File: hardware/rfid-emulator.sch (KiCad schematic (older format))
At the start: 95 parts, among them J1 AVR-JTAG-10, J2 Micro_USB, J3 OSTTC020162, Q1 2N3904, Q2 2N3906, Q3 2N3906, Q4 IRLML6344TRPBF, Q5 IRLML6344TRPBF, SW1 EN11-HSM1BF20, U1 NHD-C0216CiZ-FSW-FBW-3V3, U2 LT8613, U3 ATmega64A-AU, U4 MCP73832-2-OT, U5 LF33_TO252, U6 FT230XS, U7 LM324DT, Y1 ECS-160-20-5PX-TR

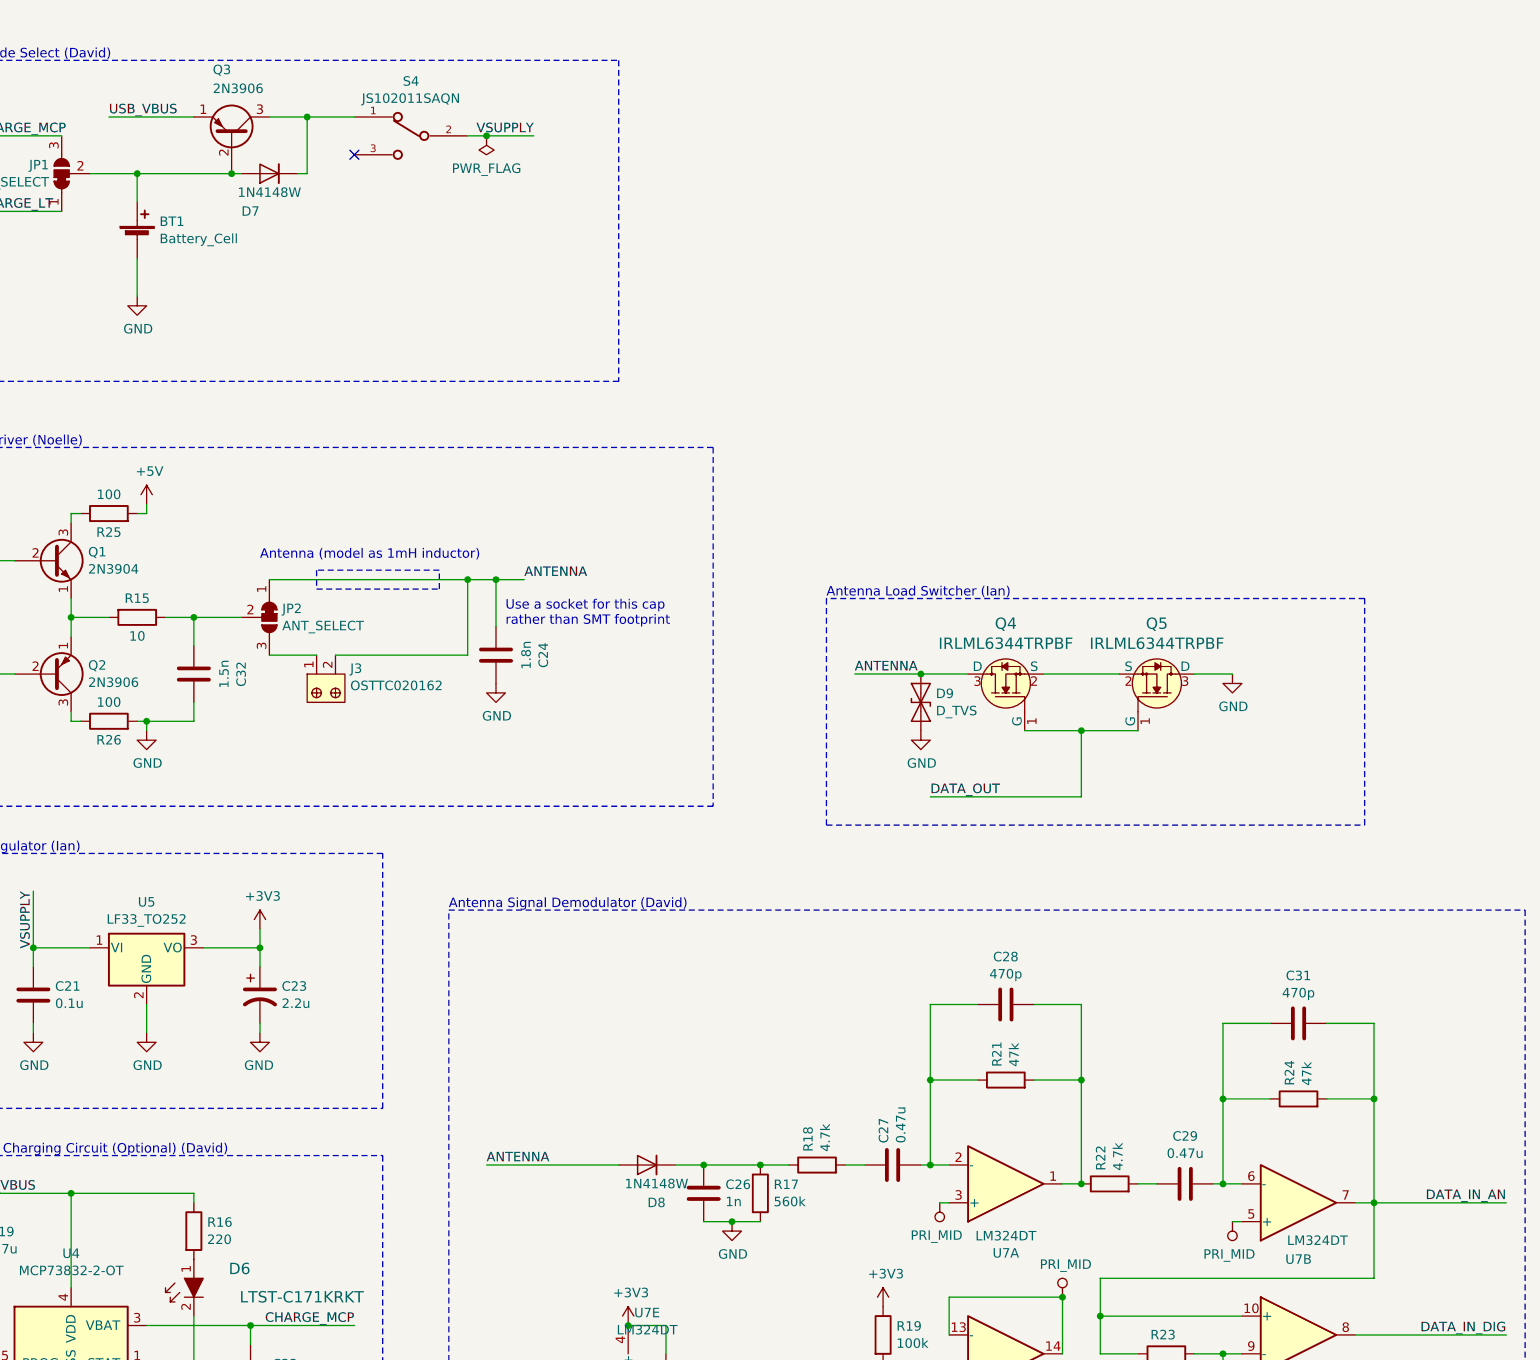
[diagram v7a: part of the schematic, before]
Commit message: Add test points and extra capacitor socket
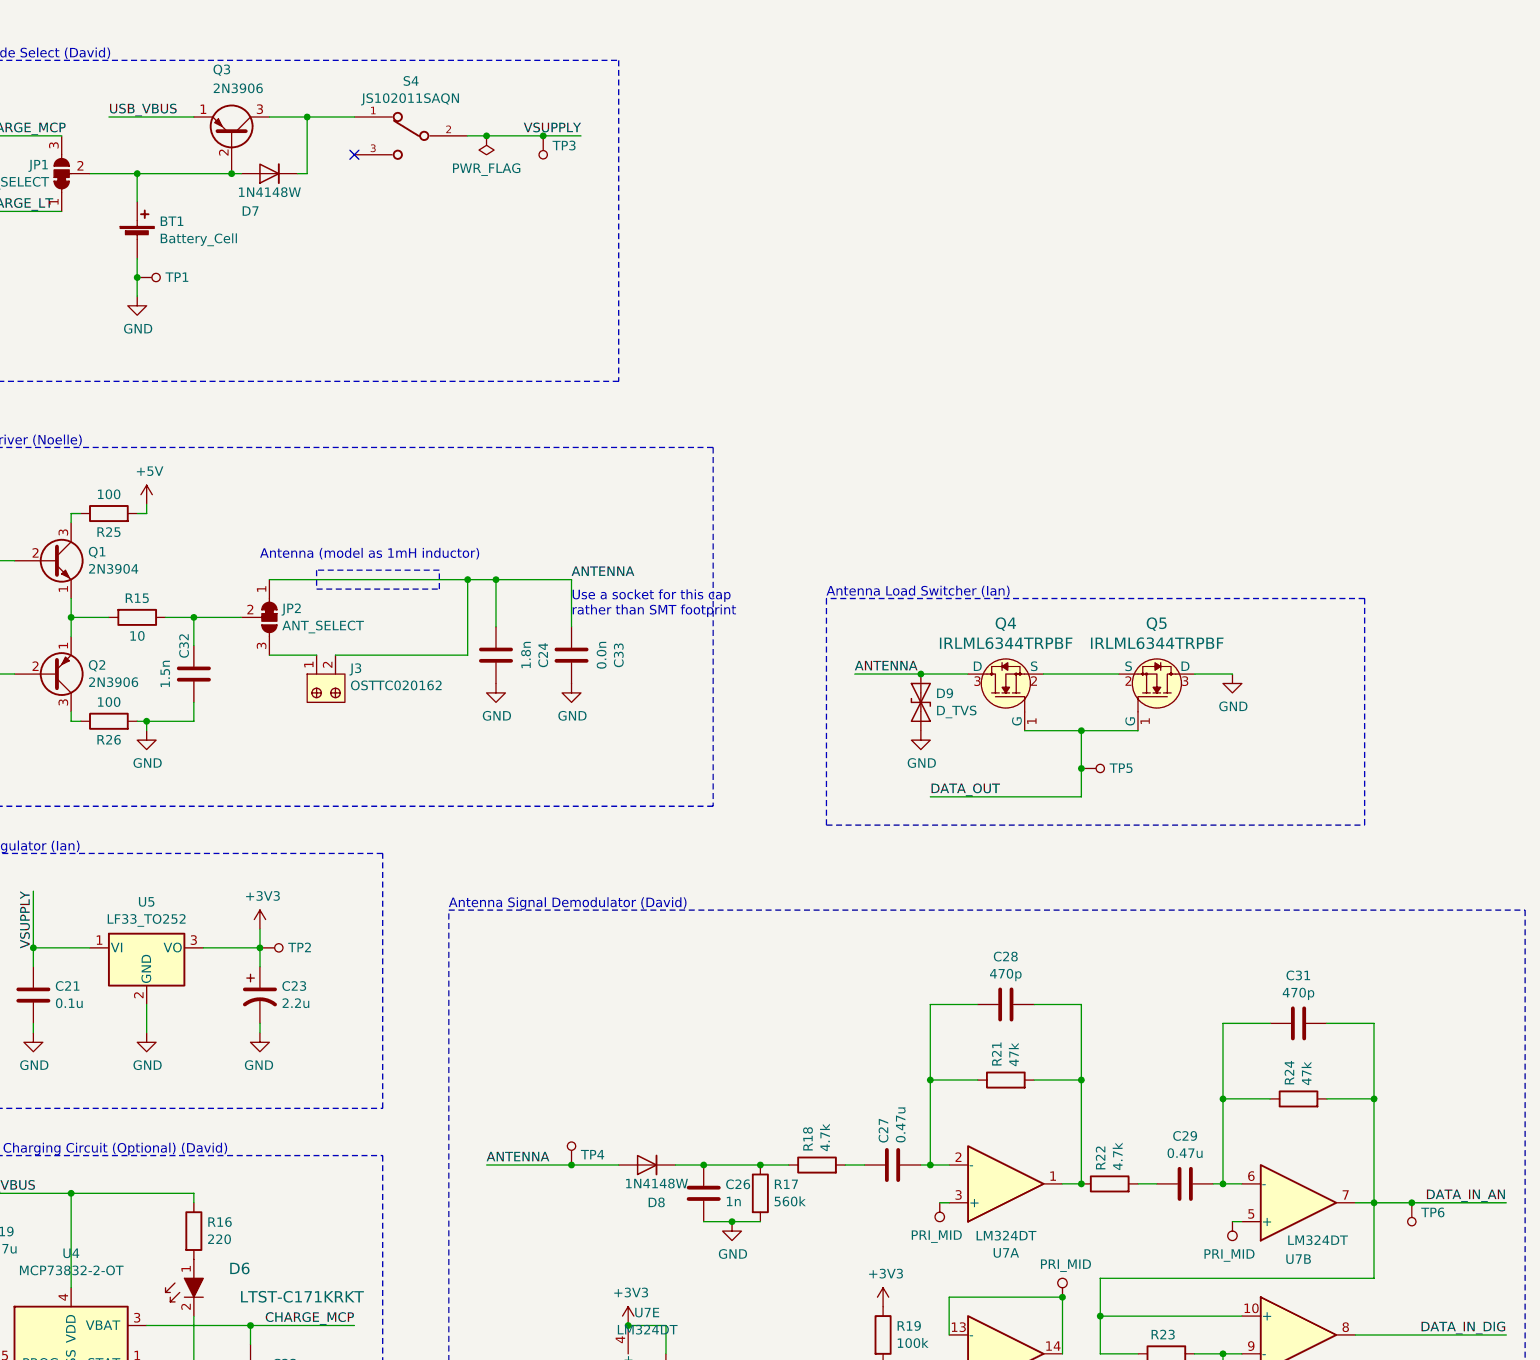
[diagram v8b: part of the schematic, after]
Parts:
- added C33: 0.0n, Socket_Strips:Socket_Strip_Straight_1x02_Pitch2.54mm, symbol Device:C
- added TP1: 5001, digikey-footprints:Test_Point_D1.02mm, symbol dk_Test-Points:5001
- added TP2, TP3: 5000, digikey-footprints:Test_Point_D1.02mm, symbol dk_Test-Points:5000
- added TP4, TP5, TP6: 5002, digikey-footprints:Test_Point_D1.02mm, symbol dk_Test-Points:5002
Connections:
- net +3V3: now also TP2.1
- net ANTENNA: now also C33.2, TP4.1
- net DATA_IN_AN: now also TP6.1
- net DATA_OUT: now also TP5.1
- net GND: now also C33.1, TP1.1
- net VSUPPLY: now also TP3.1
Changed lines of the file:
@@
 	-1   0    0    1
 $EndComp
-Text Label 10200 3650 0    50   ~ 0
+Text Label 10450 3650 0    50   ~ 0
 ANTENNA
 Wire Wire Line
-	10200 3650 10050 3650
+	10450 3650 10050 3650
 Text Label 7150 3850 0    50   ~ 0
 OC0
@@
 Wire Wire Line
 	13750 4150 13950 4150
-Wire Wire Line
-	13150 4800 13150 4450
 Wire Wire Line
 	12350 4800 13150 4800
@@
 	0    -1   -1   0
 $EndComp
-Text Notes 10100 3900 0    50   ~ 0
+Text Notes 10450 3850 0    50   ~ 0
 Use a socket for this cap\nrather than SMT footprint
 $Comp
@@
 Text Label 7250 6900 0    50   ~ 0
 USB_VBUS
-Text Label 10250 1300 2    50   ~ 0
+Text Label 10500 1300 2    50   ~ 0
 VSUPPLY
 Wire Wire Line
@@
 $EndComp
 Wire Wire Line
-	10000 6750 10700 6750
-Wire Wire Line
 	12450 7450 13050 7450
 Wire Wire Line
 	14600 7650 15400 7650
 Wire Wire Line
-	14700 6950 15400 6950
-Wire Wire Line
 	8500 5600 8800 5600
 Wire Wire Line
 	9050 1200 9300 1200
 Wire Wire Line
-	10250 1300 10000 1300
+	10500 1300 10300 1300
 Connection ~ 10000 1300
 Wire Wire Line
@@
 $EndComp
 Wire Wire Line
-	8150 1950 8150 2150
+	8150 1950 8150 2050
 Wire Wire Line
 	12300 6750 12350 6750
@@
 U 1 1 5DD510A8
 P 8450 4150
-F 0 "C32" V 8198 4150 50  0000 C CNN
-F 1 "1.5n" V 8289 4150 50  0000 C CNN
+F 0 "C32" V 8500 4000 50  0000 C CNN
+F 1 "1.5n" V 8600 4150 50  0000 C CNN
 F 2 "Capacitors_SMD:C_0805_HandSoldering" H 8488 4000 50  0001 C CNN
 F 3 "~" H 8450 4150 50  0001 C CNN
@@
 Text Notes 8800 3550 0    50   ~ 0
 Antenna (model as 1mH inductor)
+Connection ~ 8150 2050
+Wire Wire Line
+	8150 2050 8150 2150
+$Comp
+L dk_Test-Points:5001 TP1
+U 1 1 5DEB6467
+P 8250 2050
+F 0 "TP1" V 8250 2000 50  0000 R CNN
+F 1 "5001" H 8250 1950 50  0001 C CNN
+F 2 "digikey-footprints:Test_Point_D1.02mm" H 8450 2250 60  0001 L CNN
+F 3 "http://www.keyelco.com/product-pdf.cfm?p=1310" H 8450 2350 60  0001 L CNN
+F 4 "36-5001-ND" H 8450 2450 60  0001 L CNN "Digi-Key_PN"
+F 5 "5001" H 8450 2550 60  0001 L CNN "MPN"
+F 6 "Test and Measurement" H 8450 2650 60  0001 L CNN "Category"
+F 7 "Test Points" H 8450 2750 60  0001 L CNN "Family"
+F 8 "http://www.keyelco.com/product-pdf.cfm?p=1310" H 8450 2850 60  0001 L CNN "DK_Datasheet_Link"
+F 9 "/product-detail/en/keystone-electronics/5001/36-5001-ND/255327" H 8450 2950 60  0001 L CNN "DK_Detail_Page"
+F 10 "PC TEST POINT MINIATURE BLACK" H 8450 3050 60  0001 L CNN "Description"
+F 11 "Keystone Electronics" H 8450 3150 60  0001 L CNN "Manufacturer"
+F 12 "Active" H 8450 3250 60  0001 L CNN "Status"
+	1    8250 2050
+	0    -1   -1   0
+$EndComp
+$Comp
+L dk_Test-Points:5000 TP3
+U 1 1 5DED9B03
+P 10300 1400
+F 0 "TP3" H 10350 1447 50  0000 L CNN
+F 1 "5000" H 10300 1300 50  0001 C CNN
+F 2 "digikey-footprints:Test_Point_D1.02mm" H 10500 1600 60  0001 L CNN
+F 3 "http://www.keyelco.com/product-pdf.cfm?p=1309" H 10500 1700 60  0001 L CNN
+F 4 "36-5000-ND" H 10500 1800 60  0001 L CNN "Digi-Key_PN"
+F 5 "5000" H 10500 1900 60  0001 L CNN "MPN"
+F 6 "Test and Measurement" H 10500 2000 60  0001 L CNN "Category"
+F 7 "Test Points" H 10500 2100 60  0001 L CNN "Family"
+F 8 "http://www.keyelco.com/product-pdf.cfm?p=1309" H 10500 2200 60  0001 L CNN "DK_Datasheet_Link"
+F 9 "/product-detail/en/keystone-electronics/5000/36-5000-ND/255326" H 10500 2300 60  0001 L CNN "DK_Detail_Page"
+F 10 "PC TEST POINT MINIATURE RED" H 10500 2400 60  0001 L CNN "Description"
+F 11 "Keystone Electronics" H 10500 2500 60  0001 L CNN "Manufacturer"
+F 12 "Active" H 10500 2600 60  0001 L CNN "Status"
+	1    10300 1400
+	1    0    0    -1
+$EndComp
+Connection ~ 10300 1300
+Wire Wire Line
+	10300 1300 10000 1300
+$Comp
+L dk_Test-Points:5000 TP2
+U 1 1 5DEDB0EF
+P 8900 5600
+F 0 "TP2" V 8900 5550 50  0000 R CNN
+F 1 "5000" H 8900 5500 50  0001 C CNN
+F 2 "digikey-footprints:Test_Point_D1.02mm" H 9100 5800 60  0001 L CNN
+F 3 "http://www.keyelco.com/product-pdf.cfm?p=1309" H 9100 5900 60  0001 L CNN
+F 4 "36-5000-ND" H 9100 6000 60  0001 L CNN "Digi-Key_PN"
+F 5 "5000" H 9100 6100 60  0001 L CNN "MPN"
+F 6 "Test and Measurement" H 9100 6200 60  0001 L CNN "Category"
+F 7 "Test Points" H 9100 6300 60  0001 L CNN "Family"
+F 8 "http://www.keyelco.com/product-pdf.cfm?p=1309" H 9100 6400 60  0001 L CNN "DK_Datasheet_Link"
+F 9 "/product-detail/en/keystone-electronics/5000/36-5000-ND/255326" H 9100 6500 60  0001 L CNN "DK_Detail_Page"
+F 10 "PC TEST POINT MINIATURE RED" H 9100 6600 60  0001 L CNN "Description"
+F 11 "Keystone Electronics" H 9100 6700 60  0001 L CNN "Manufacturer"
+F 12 "Active" H 9100 6800 60  0001 L CNN "Status"
+	1    8900 5600
+	0    -1   -1   0
+$EndComp
+$Comp
+L dk_Test-Points:5002 TP4
+U 1 1 5DEE53AA
+P 10450 6650
+F 0 "TP4" H 10400 6697 50  0000 R CNN
+F 1 "5002" H 10450 6550 50  0001 C CNN
+F 2 "digikey-footprints:Test_Point_D1.02mm" H 10650 6850 60  0001 L CNN
+F 3 "http://www.keyelco.com/product-pdf.cfm?p=1311" H 10650 6950 60  0001 L CNN
+F 4 "36-5002-ND" H 10650 7050 60  0001 L CNN "Digi-Key_PN"
+F 5 "5002" H 10650 7150 60  0001 L CNN "MPN"
+F 6 "Test and Measurement" H 10650 7250 60  0001 L CNN "Category"
+F 7 "Test Points" H 10650 7350 60  0001 L CNN "Family"
+F 8 "http://www.keyelco.com/product-pdf.cfm?p=1311" H 10650 7450 60  0001 L CNN "DK_Datasheet_Link"
+F 9 "/product-detail/en/keystone-electronics/5002/36-5002-ND/255328" H 10650 7550 60  0001 L CNN "DK_Detail_Page"
+F 10 "PC TEST POINT MINIATURE WHITE" H 10650 7650 60  0001 L CNN "Description"
+F 11 "Keystone Electronics" H 10650 7750 60  0001 L CNN "Manufacturer"
+F 12 "Active" H 10650 7850 60  0001 L CNN "Status"
+	1    10450 6650
+	-1   0    0    1
+$EndComp
+Wire Wire Line
+	10000 6750 10450 6750
+Connection ~ 10450 6750
+Wire Wire Line
+	10450 6750 10700 6750
+$Comp
+L dk_Test-Points:5002 TP6
+U 1 1 5DEECD7B
+P 14900 7050
+F 0 "TP6" H 14950 7097 50  0000 L CNN
+F 1 "5002" H 14900 6950 50  0001 C CNN
+F 2 "digikey-footprints:Test_Point_D1.02mm" H 15100 7250 60  0001 L CNN
+F 3 "http://www.keyelco.com/product-pdf.cfm?p=1311" H 15100 7350 60  0001 L CNN
+F 4 "36-5002-ND" H 15100 7450 60  0001 L CNN "Digi-Key_PN"
+F 5 "5002" H 15100 7550 60  0001 L CNN "MPN"
+F 6 "Test and Measurement" H 15100 7650 60  0001 L CNN "Category"
+F 7 "Test Points" H 15100 7750 60  0001 L CNN "Family"
+F 8 "http://www.keyelco.com/product-pdf.cfm?p=1311" H 15100 7850 60  0001 L CNN "DK_Datasheet_Link"
+F 9 "/product-detail/en/keystone-electronics/5002/36-5002-ND/255328" H 15100 7950 60  0001 L CNN "DK_Detail_Page"
+F 10 "PC TEST POINT MINIATURE WHITE" H 15100 8050 60  0001 L CNN "Description"
+F 11 "Keystone Electronics" H 15100 8150 60  0001 L CNN "Manufacturer"
+F 12 "Active" H 15100 8250 60  0001 L CNN "Status"
+	1    14900 7050
+	1    0    0    -1
+$EndComp
+Wire Wire Line
+	14700 6950 14900 6950
+Connection ~ 14900 6950
+Wire Wire Line
+	14900 6950 15400 6950
+$Comp
+L dk_Test-Points:5002 TP5
+U 1 1 5DEF5A30
+P 13250 4650
+F 0 "TP5" V 13250 4600 50  0000 R CNN
+F 1 "5002" H 13250 4550 50  0001 C CNN
+F 2 "digikey-footprints:Test_Point_D1.02mm" H 13450 4850 60  0001 L CNN
+F 3 "http://www.keyelco.com/product-pdf.cfm?p=1311" H 13450 4950 60  0001 L CNN
+F 4 "36-5002-ND" H 13450 5050 60  0001 L CNN "Digi-Key_PN"
+F 5 "5002" H 13450 5150 60  0001 L CNN "MPN"
+F 6 "Test and Measurement" H 13450 5250 60  0001 L CNN "Category"
+F 7 "Test Points" H 13450 5350 60  0001 L CNN "Family"
+F 8 "http://www.keyelco.com/product-pdf.cfm?p=1311" H 13450 5450 60  0001 L CNN "DK_Datasheet_Link"
+F 9 "/product-detail/en/keystone-electronics/5002/36-5002-ND/255328" H 13450 5550 60  0001 L CNN "DK_Detail_Page"
+F 10 "PC TEST POINT MINIATURE WHITE" H 13450 5650 60  0001 L CNN "Description"
+F 11 "Keystone Electronics" H 13450 5750 60  0001 L CNN "Manufacturer"
+F 12 "Active" H 13450 5850 60  0001 L CNN "Status"
+	1    13250 4650
+	0    -1   -1   0
+$EndComp
+Wire Wire Line
+	13150 4450 13150 4650
+Connection ~ 13150 4650
+Wire Wire Line
+	13150 4650 13150 4800
+$Comp
+L Device:C C33
+U 1 1 5DF88A4E
+P 10450 4050
+F 0 "C33" V 10198 4050 50  0000 C CNN
+F 1 "0.0n" V 10289 4050 50  0000 C CNN
+F 2 "Socket_Strips:Socket_Strip_Straight_1x02_Pitch2.54mm" H 10488 3900 50  0001 C CNN
+F 3 "~" H 10450 4050 50  0001 C CNN
+	1    10450 4050
+	-1   0    0    1
+$EndComp
+Wire Wire Line
+	10450 3900 10450 3650
+$Comp
+L power:GND #PWR051
+U 1 1 5DFAA0F3
+P 10450 4200
+F 0 "#PWR051" H 10450 3950 50  0001 C CNN
+F 1 "GND" H 10455 4027 50  0000 C CNN
+F 2 "" H 10450 4200 50  0001 C CNN
+F 3 "" H 10450 4200 50  0001 C CNN
+	1    10450 4200
+	1    0    0    -1
+$EndComp
 $EndSCHEMATC
